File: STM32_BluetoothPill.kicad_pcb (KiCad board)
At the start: 2 copper layers, 1 part, among them U1 STM32WBxx

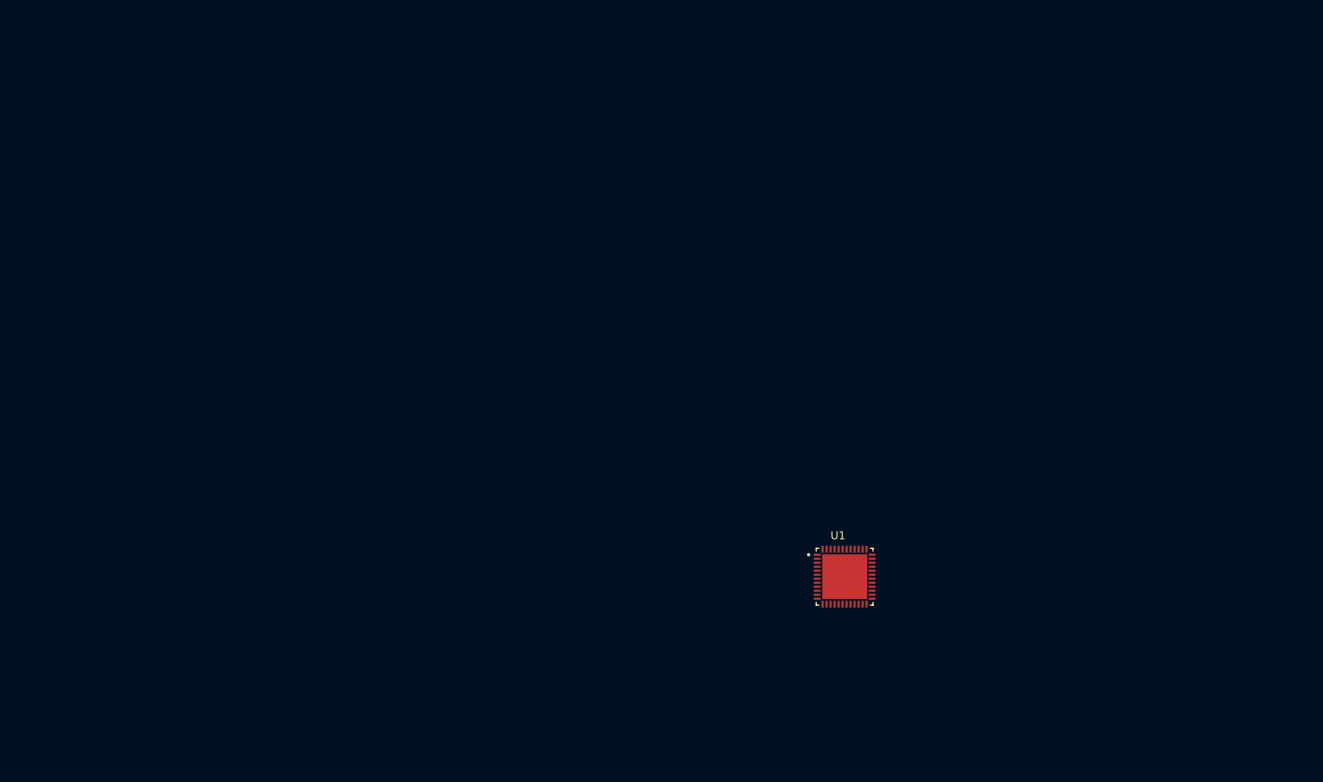
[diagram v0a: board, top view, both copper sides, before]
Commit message: footprints designated
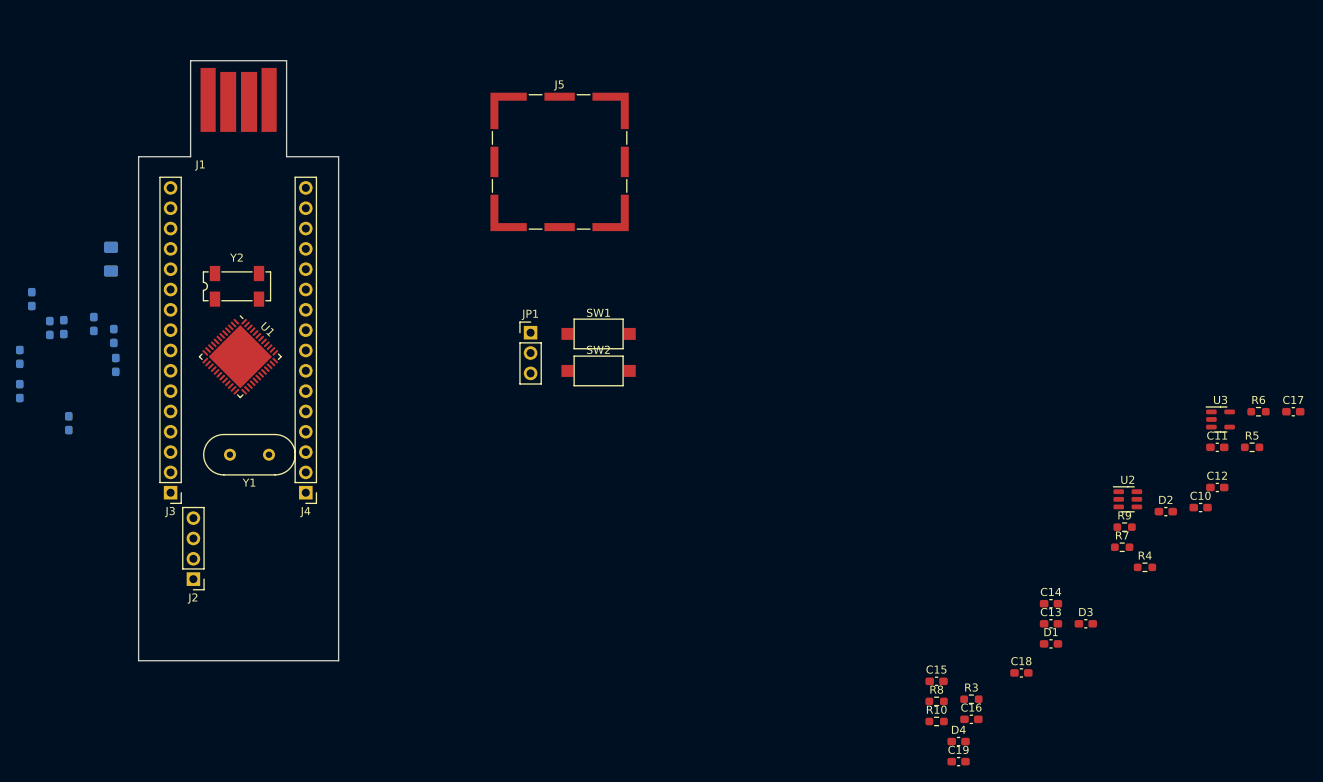
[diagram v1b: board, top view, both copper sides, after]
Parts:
- added C1: 100n, Capacitor_SMD:C_0603_1608Metric_Pad1.08x0.95mm_HandSolder, B.Cu at (27.1, 56.0)
- added C10: 12p, Capacitor_SMD:C_0603_1608Metric_Pad1.08x0.95mm_HandSolder, F.Cu at (162.8, 73.9)
- added C11: 12p, Capacitor_SMD:C_0603_1608Metric_Pad1.08x0.95mm_HandSolder, F.Cu at (164.8, 66.3)
- added C12: 10p, Capacitor_SMD:C_0603_1608Metric_Pad1.08x0.95mm_HandSolder, F.Cu at (164.8, 71.3)
- added C13: 10p, Capacitor_SMD:C_0603_1608Metric_Pad1.08x0.95mm_HandSolder, F.Cu at (144.1, 88.4)
- added C14: 1u, Capacitor_SMD:C_0603_1608Metric_Pad1.08x0.95mm_HandSolder, F.Cu at (144.1, 85.9)
- added C15: 100n, Capacitor_SMD:C_0603_1608Metric_Pad1.08x0.95mm_HandSolder, F.Cu at (129.8, 95.6)
- added C16: 10n, Capacitor_SMD:C_0603_1608Metric_Pad1.08x0.95mm_HandSolder, F.Cu at (134.1, 100.3)
- added C17: 1u, Capacitor_SMD:C_0603_1608Metric_Pad1.08x0.95mm_HandSolder, F.Cu at (174.3, 61.9)
- added C18: 100n, Capacitor_SMD:C_0603_1608Metric_Pad1.08x0.95mm_HandSolder, F.Cu at (140.3, 94.5)
- added C19: 100n, Capacitor_SMD:C_0603_1608Metric_Pad1.08x0.95mm_HandSolder, F.Cu at (132.5, 105.6)
- added C2: 100n, Capacitor_SMD:C_0603_1608Metric_Pad1.08x0.95mm_HandSolder, B.Cu at (18.9, 51.4)
- added C3: 100n, Capacitor_SMD:C_0603_1608Metric_Pad1.08x0.95mm_HandSolder, B.Cu at (15.2, 59.3)
- added C4: 100n, Capacitor_SMD:C_0603_1608Metric_Pad1.08x0.95mm_HandSolder, B.Cu at (21.3, 63.3)
- added C5: 100n, Capacitor_SMD:C_0603_1608Metric_Pad1.08x0.95mm_HandSolder, B.Cu at (15.2, 55.0)
- added C6: 4.7u, Capacitor_SMD:C_0603_1608Metric_Pad1.08x0.95mm_HandSolder, B.Cu at (20.6, 51.3)
- added C7: 100n, Capacitor_SMD:C_0603_1608Metric_Pad1.08x0.95mm_HandSolder, B.Cu at (26.9, 52.4)
- added C8: 100p, Capacitor_SMD:C_0603_1608Metric_Pad1.08x0.95mm_HandSolder, B.Cu at (24.4, 50.9)
- added C9: 4.7u, Capacitor_SMD:C_0603_1608Metric_Pad1.08x0.95mm_HandSolder, B.Cu at (16.6, 47.8)
- added D1: GRN, Capacitor_SMD:C_0603_1608Metric_Pad1.08x0.95mm_HandSolder, F.Cu at (144.1, 90.9)
- added D2: RED, Capacitor_SMD:C_0603_1608Metric_Pad1.08x0.95mm_HandSolder, F.Cu at (158.4, 74.4)
- added D3: BLU, Capacitor_SMD:C_0603_1608Metric_Pad1.08x0.95mm_HandSolder, F.Cu at (148.4, 88.4)
- added D4: PWR, Capacitor_SMD:C_0603_1608Metric_Pad1.08x0.95mm_HandSolder, F.Cu at (132.5, 103.1)
- added J1: USB_A, lib:CONN-USB-A-PCB-TRACES, F.Cu at (42.5, 18.0)
- added J2: Conn, Connector_PinHeader_2.54mm:PinHeader_1x04_P2.54mm_Vertical, F.Cu at (36.9, 82.8)
- added J3: Conn, Connector_PinHeader_2.54mm:PinHeader_1x16_P2.54mm_Vertical, F.Cu at (34.0, 72.0)
- added J4: Conn, Connector_PinHeader_2.54mm:PinHeader_1x16_P2.54mm_Vertical, F.Cu at (50.9, 72.0)
- added J5: RFShield, RF_Shielding:Laird_Technologies_BMI-S-202-F_16.50x16.50mm, F.Cu at (82.6, 30.6)
- added JP1: Jumper_3_Open, Connector_PinHeader_2.54mm:PinHeader_1x03_P2.54mm_Vertical, F.Cu at (79.0, 52.0)
- added L1: 10u, Inductor_SMD:L_1206_3216Metric_Pad1.42x1.75mm_HandSolder, B.Cu at (26.6, 42.8)
- added R10: 680, Resistor_SMD:R_0603_1608Metric_Pad0.98x0.95mm_HandSolder, F.Cu at (129.8, 100.6)
- added R3: NC, Resistor_SMD:R_0603_1608Metric_Pad0.98x0.95mm_HandSolder, F.Cu at (134.1, 97.8)
- added R4: 0, Resistor_SMD:R_0603_1608Metric_Pad0.98x0.95mm_HandSolder, F.Cu at (155.8, 81.3)
- added R5: 10k, Resistor_SMD:R_0603_1608Metric_Pad0.98x0.95mm_HandSolder, F.Cu at (169.2, 66.3)
- added R6: 1k, Resistor_SMD:R_0603_1608Metric_Pad0.98x0.95mm_HandSolder, F.Cu at (170.0, 61.9)
- added R7: 680, Resistor_SMD:R_0603_1608Metric_Pad0.98x0.95mm_HandSolder, F.Cu at (152.9, 78.8)
- added R8: 680, Resistor_SMD:R_0603_1608Metric_Pad0.98x0.95mm_HandSolder, F.Cu at (129.8, 98.1)
- added R9: 680, Resistor_SMD:R_0603_1608Metric_Pad0.98x0.95mm_HandSolder, F.Cu at (153.2, 76.3)
- added SW1: Reset, Button_Switch_SMD:SW_SPST_CK_RS282G05A3, F.Cu at (87.5, 52.1)
- added SW2: User PB, Button_Switch_SMD:SW_SPST_CK_RS282G05A3, F.Cu at (87.5, 56.8)
- added U2: USBLC6-2SC6, Package_TO_SOT_SMD:SOT-23-6, F.Cu at (153.7, 72.8)
- added U3: LD3985M33R_SOT23, Package_TO_SOT_SMD:SOT-23-5, F.Cu at (165.2, 62.8)
- added Y1: 8M, Crystal:Crystal_HC49-4H_Vertical, F.Cu at (46.3, 67.2)
- added Y2: 32k768, Crystal:Crystal_SMD_SeikoEpson_MC306-4Pin_8.0x3.2mm, F.Cu at (42.3, 46.2)
- U1: footprint lib:QFN50P700X700X60-49N -> Package_DFN_QFN:QFN-48-1EP_7x7mm_P0.5mm_EP5.6x5.6mm
- moved U1 80.4 mm to (42.7, 55.0), turned to -45 degrees
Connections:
- U1 pad 10: unconnected-(U1-Pad10) -> PA1
- U1 pad 11: unconnected-(U1-Pad11) -> PA2
- U1 pad 12: unconnected-(U1-Pad12) -> PA3
- U1 pad 13: unconnected-(U1-Pad13) -> PA4
- U1 pad 14: unconnected-(U1-Pad14) -> PA5
- U1 pad 15: unconnected-(U1-Pad15) -> PA6
- U1 pad 16: unconnected-(U1-Pad16) -> PA7
- U1 pad 17: unconnected-(U1-Pad17) -> PA8
- U1 pad 18: unconnected-(U1-Pad18) -> PA9
- U1 pad 19: unconnected-(U1-Pad19) -> PB2
- U1 pad 2: unconnected-(U1-Pad2) -> Net-(C13-Pad1)
- U1 pad 20: Net-(U1-Pad20) -> +3V3
- U1 pad 22: unconnected-(U1-Pad22) -> GND
- U1 pad 23: unconnected-(U1-Pad23) -> +3V3
- U1 pad 24: unconnected-(U1-Pad24) -> Net-(C11-Pad1)
- U1 pad 25: unconnected-(U1-Pad25) -> Net-(C10-Pad1)
- U1 pad 28: unconnected-(U1-Pad28) -> PB0
- U1 pad 29: unconnected-(U1-Pad29) -> PB1
- U1 pad 3: unconnected-(U1-Pad3) -> Net-(C12-Pad1)
- U1 pad 30: unconnected-(U1-Pad30) -> PE4
- U1 pad 31: unconnected-(U1-Pad31) -> Net-(C9-Pad2)
- U1 pad 32: unconnected-(U1-Pad32) -> GND
- U1 pad 33: unconnected-(U1-Pad33) -> Net-(L1-Pad1)
- U1 pad 34: unconnected-(U1-Pad34) -> +3V3
- U1 pad 35: Net-(U1-Pad20) -> +3V3
- U1 pad 36: unconnected-(U1-Pad36) -> PA10
- U1 pad 37: unconnected-(U1-Pad37) -> USB_N
- U1 pad 38: unconnected-(U1-Pad38) -> USB_P
- U1 pad 39: unconnected-(U1-Pad39) -> SWDIO
- U1 pad 4: unconnected-(U1-Pad4) -> Net-(JP1-Pad2)
- U1 pad 40: unconnected-(U1-Pad40) -> +3V3
- U1 pad 41: unconnected-(U1-Pad41) -> SWCLK
- U1 pad 42: unconnected-(U1-Pad42) -> PA15
- U1 pad 43: unconnected-(U1-Pad43) -> PB3
- U1 pad 44: unconnected-(U1-Pad44) -> PB4
- U1 pad 45: unconnected-(U1-Pad45) -> PB5
- U1 pad 46: unconnected-(U1-Pad46) -> PB6
- U1 pad 47: unconnected-(U1-Pad47) -> PB7
- U1 pad 48: Net-(U1-Pad20) -> +3V3
- U1 pad 49: unconnected-(U1-Pad49) -> GND
- U1 pad 5: unconnected-(U1-Pad5) -> PB8
- U1 pad 6: unconnected-(U1-Pad6) -> PB9
- U1 pad 7: unconnected-(U1-Pad7) -> RESET
- U1 pad 8: unconnected-(U1-Pad8) -> +3V3
- U1 pad 9: unconnected-(U1-Pad9) -> PA0
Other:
- board outline added: 25 x 75 mm

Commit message: pcb parts placement
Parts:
- C10, C12, C13, C14, C15, C16, C17, C18, C19, R3, R4, R5, R6, R7, R8, U2, U3: moved to B.Cu
- moved C17 138.0 mm to (38.2, 38.8), turned to 180 degrees
- moved C12 128.7 mm to (38.4, 47.2)
- moved R5 128.6 mm to (41.5, 51.2), turned to 180 degrees
- moved U3 128.6 mm to (40.2, 32.8), turned to -90 degrees
- moved C11 126.6 mm to (38.2, 64.2), turned to 90 degrees
- moved R6 126.4 mm to (45.5, 40.2)
- moved R4 121.6 mm to (41.5, 39.8), turned to 90 degrees
- moved C10 120.4 mm to (42.8, 64.2), turned to 90 degrees
- moved C18 117.4 mm to (38.2, 36.5), turned to 180 degrees
- moved D2 115.9 mm to (42.6, 69.8), turned to 180 degrees
- moved D4 115.7 mm to (38.8, 35.4), turned to -90 degrees
- moved R7 114.6 mm to (38.8, 69.8)
- moved U2 114.2 mm to (46.8, 32.8), turned to -90 degrees
- moved C14 113.4 mm to (43.5, 33.5), turned to -90 degrees
- moved C15 111.9 mm to (37.0, 33.0), turned to -90 degrees
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
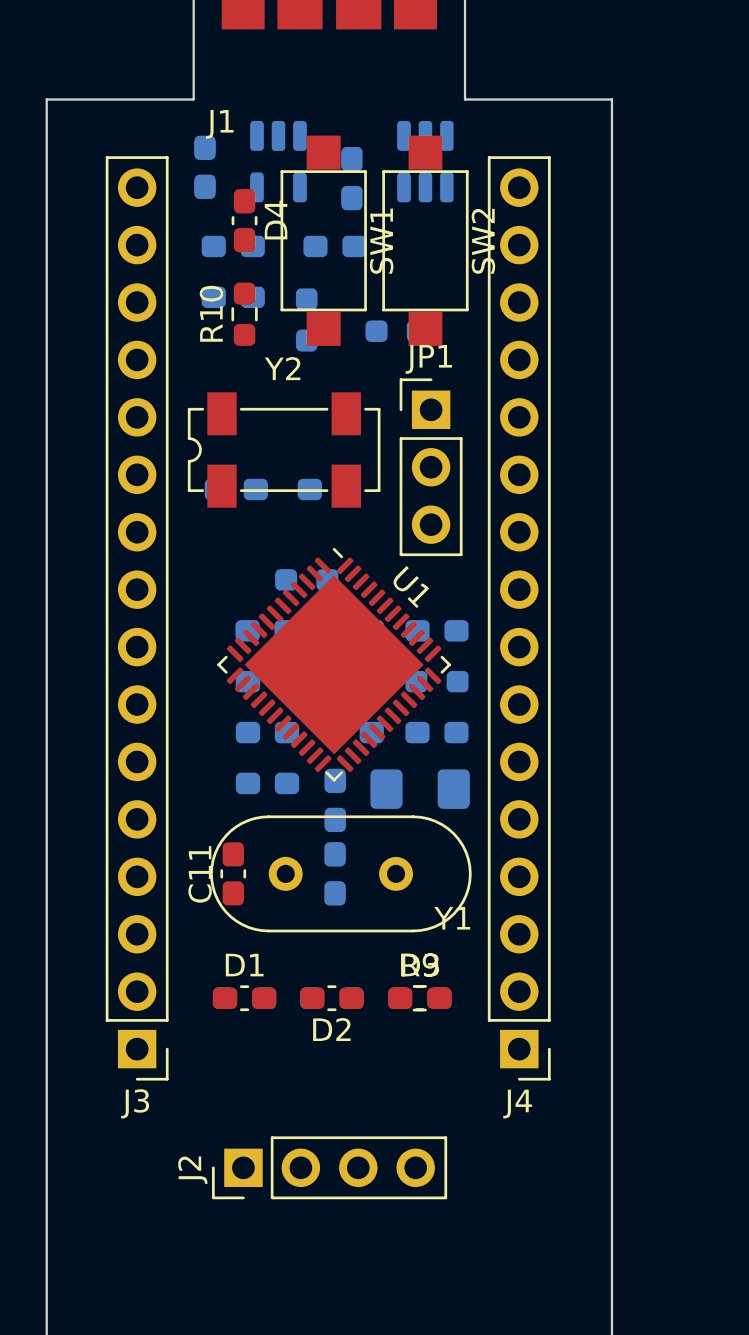
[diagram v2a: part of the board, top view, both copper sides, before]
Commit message: footprints changed gpio names added
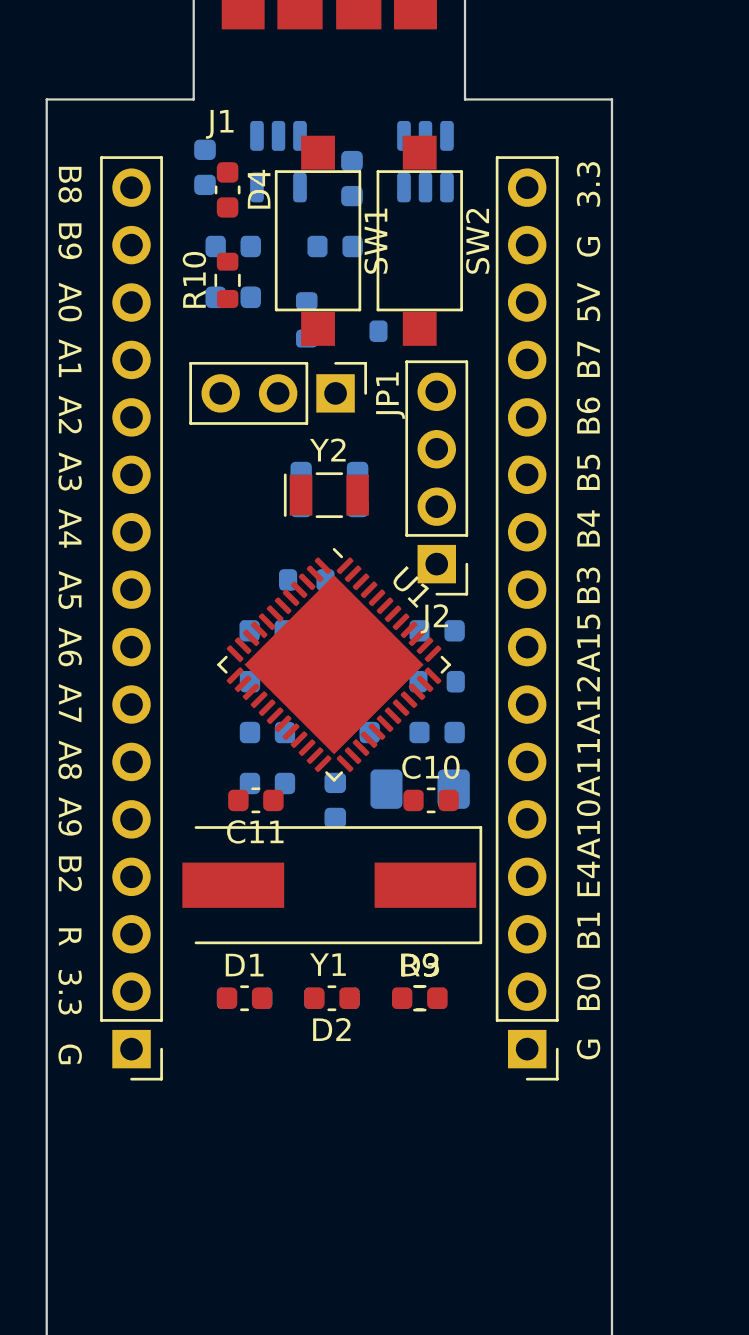
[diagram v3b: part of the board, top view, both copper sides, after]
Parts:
- C1, C11, C12, C13, C14, C15, C16, C17, C18, C19, C2, C3, C4, C5, C6, C7, C8, C9, D1, D2, D3, D4: footprint Capacitor_SMD:C_0603_1608Metric_Pad1.08x0.95mm_HandSolder -> Capacitor_SMD:C_0603_1608Metric
- C10: footprint Capacitor_SMD:C_0603_1608Metric_Pad1.08x0.95mm_HandSolder -> Capacitor_SMD:C_0603_1608Metric; moved to F.Cu
- R10, R3, R4, R5, R6, R7, R8, R9: footprint Resistor_SMD:R_0603_1608Metric_Pad0.98x0.95mm_HandSolder -> Resistor_SMD:R_0603_1608Metric
- Y1: footprint Crystal:Crystal_HC49-4H_Vertical -> Crystal:Crystal_SMD_HC49-SD
- Y2: footprint Crystal:Crystal_SMD_SeikoEpson_MC306-4Pin_8.0x3.2mm -> Crystal:Crystal_SMD_G8-2Pin_3.2x1.5mm
- moved J2 28.0 mm to (47.2, 50.5), turned to 180 degrees
- moved C10 5.35 mm to (47.0, 61.0), turned to 0 degrees
- moved JP1 4.29 mm to (42.8, 43.0), turned to -90 degrees
- moved C11 3.40 mm to (39.2, 61.0), turned to 180 degrees
- moved Y1 2.99 mm to (42.5, 64.8)
- moved C12 2.86 mm to (41.2, 47.2), turned to 90 degrees
- moved Y2 2.83 mm to (42.5, 47.5)
- moved R10 1.68 mm to (38.0, 38.0)
- moved D4 1.56 mm to (38.0, 34.0)
- moved C13 1.25 mm to (43.8, 47.2), turned to 90 degrees
- moved J4 0.35 mm to (51.2, 72.0)
- moved J3 0.25 mm to (33.8, 72.0)
- moved SW1 0.25 mm to (42.0, 36.2)
- moved SW2 0.25 mm to (46.5, 36.2)
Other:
- board text added: "3.3"
- board text added: "5V"
- board text added: "A0"
- board text added: "A1"
- board text added: "A10"
- board text added: "A11"
- board text added: "A12"
- board text added: "A15"
- board text added: "A2"
- board text added: "A3"
- board text added: "A4"
- board text added: "A5"
- board text added: "A6"
- board text added: "A7"
- board text added: "A8"
- board text added: "A9"
- board text added: "B0"
- board text added: "B1"
- board text added: "B2"
- board text added: "B3"
- board text added: "B4"
- board text added: "B5"
- board text added: "B6"
- board text added: "B7"
- board text added: "B8"
- board text added: "B9"
- board text added: "E4"
- board text added: "G"
- board text added: "R"
